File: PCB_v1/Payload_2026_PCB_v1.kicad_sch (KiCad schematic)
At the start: 9 parts, among them J1 SD Card Reader, J2 Ozone Sensor, J3 SGP40 VOC Sensor, J4 IMU, J5 BME/BMP280, J6 Ultrasonic Sensor 1, J7 Ultrasonic Sensor 2, J8 Ultrasonic Sensor 3

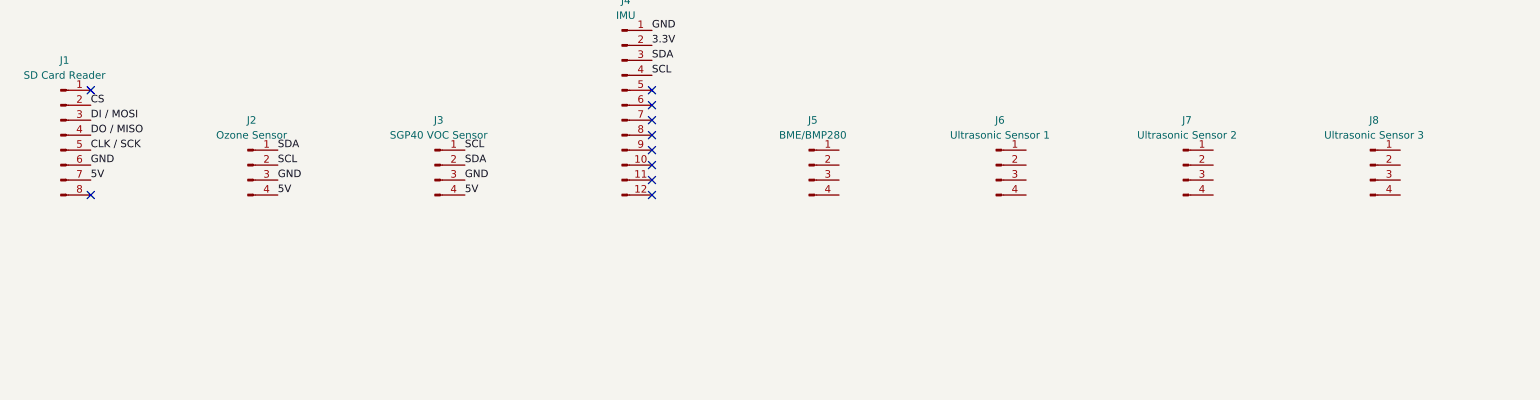
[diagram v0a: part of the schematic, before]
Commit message: PCB Footprints finished
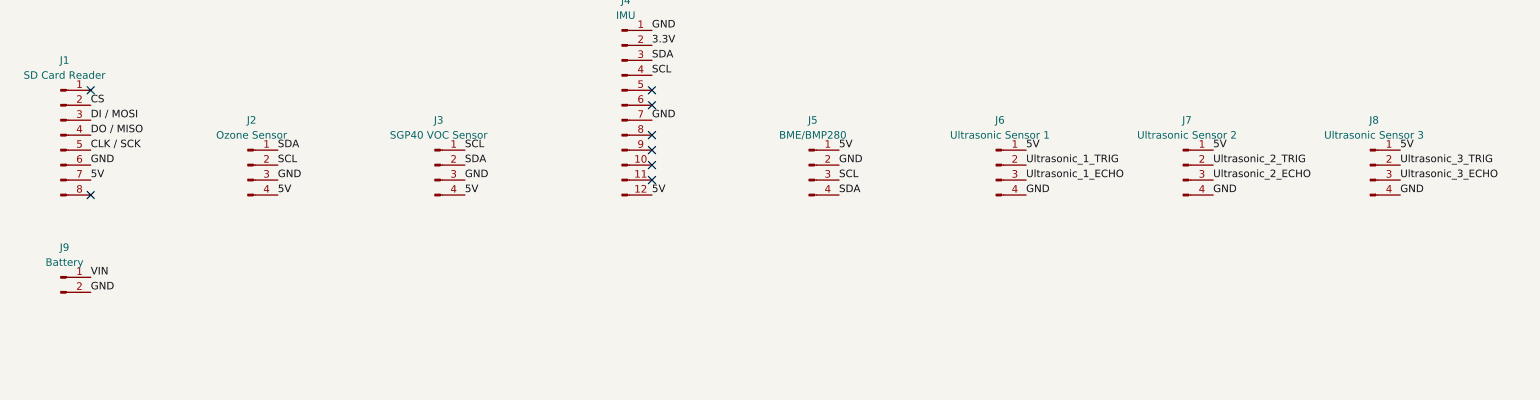
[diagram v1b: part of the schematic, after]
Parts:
- added J9: Battery, Payload_2026_PCB_v1:Battery, symbol Connector:Conn_01x02_Pin
- J1: footprint (none) -> Payload_2026_PCB_v1:SD_Card_Reader
- J2, J3, J6, J7, J8: footprint (none) -> Payload_2026_PCB_v1:Conn_01x04_Pin
- J4: footprint (none) -> Payload_2026_PCB_v1:IMU
- J5: footprint (none) -> Payload_2026_PCB_v1:BME280_Sensor
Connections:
- net 5V: now also J4.12 (Pin_12), J5.1 (Pin_1), J6.1 (Pin_1), J7.1 (Pin_1), J8.1 (Pin_1)
- net GND: now also J4.7 (Pin_7), J5.2 (Pin_2), J6.4 (Pin_4), J7.4 (Pin_4), J8.4 (Pin_4), J9.2 (Pin_2)
- net SCL: now also J5.3 (Pin_3)
- net SDA: now also J5.4 (Pin_4)
- net Ultrasonic_1_ECHO: now also J6.3 (Pin_3)
- net Ultrasonic_1_TRIG: now also J6.2 (Pin_2)
- net Ultrasonic_2_ECHO: now also J7.3 (Pin_3)
- net Ultrasonic_2_TRIG: now also J7.2 (Pin_2)
- net Ultrasonic_3_ECHO: now also J8.3 (Pin_3)
- net Ultrasonic_3_TRIG: now also J8.2 (Pin_2)
- net VIN: now also J9.1 (Pin_1)
- no-connect marks 23 -> 21

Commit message: Finish PCB Design
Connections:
- net 5V: now also J1.8 (Pin_8); no longer J1.7 (Pin_7)
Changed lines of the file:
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@@
-	)
-	(no_connect
-		(at 31.75 127)
 	)
 	(no_connect
 		(at 49.53 39.37)
+	)
+	(no_connect
+		(at 31.75 124.46)
 	)
 	(no_connect
@@
 		)
 	)
-	(label "5V"
-		(at 31.75 124.46 0)
-		(effects
-			(font
-				(size 1.27 1.27)
-			)
-			(justify left bottom)
-		)
-	)
 	(label "CS"
 		(at 31.75 111.76 0)
@@
 		)
 	)
+	(label "5V"
+		(at 31.75 127 0)
+		(effects
+			(font
+				(size 1.27 1.27)
+			)
+			(justify left bottom)
+		)
+	)

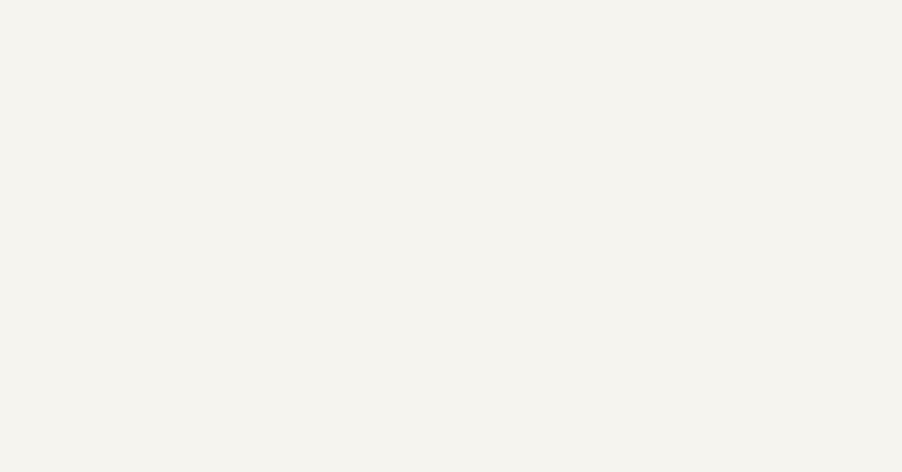
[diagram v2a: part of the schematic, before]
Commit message: Write DOTO List in sch
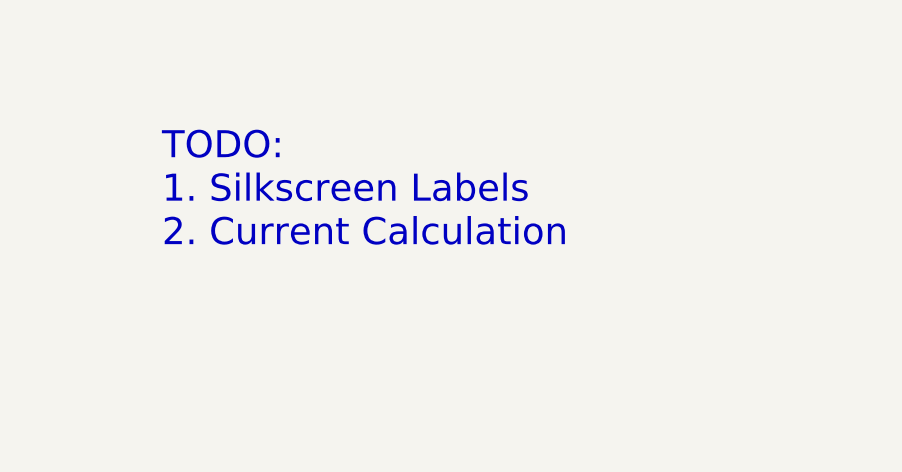
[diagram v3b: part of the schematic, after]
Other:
- note added: "TODO: 1. Silkscreen Labels 2. Current Calculation"
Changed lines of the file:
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@@
+		)
+	)
+	(text "TODO:\n1. Silkscreen Labels\n2. Current Calculation"
+		(exclude_from_sim no)
+		(at 104.648 38.862 0)
+		(effects
+			(font
+				(size 3 3)
+			)
+			(justify left top)
 		)
 	)

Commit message: Update PCB layout
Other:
- note added: "TODO: 1. Silkscreen Labels 2. Current Calculation 3. 2 Types of Pad Colors"
- note removed: "TODO: 1. Silkscreen Labels 2. Current Calculation"
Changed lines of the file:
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@@
 		)
 	)
-	(text "TODO:\n1. Silkscreen Labels\n2. Current Calculation"
+	(text "TODO:\n1. Silkscreen Labels\n2. Current Calculation\n3. 2 Types of Pad Colors"
 		(exclude_from_sim no)
 		(at 104.648 38.862 0)

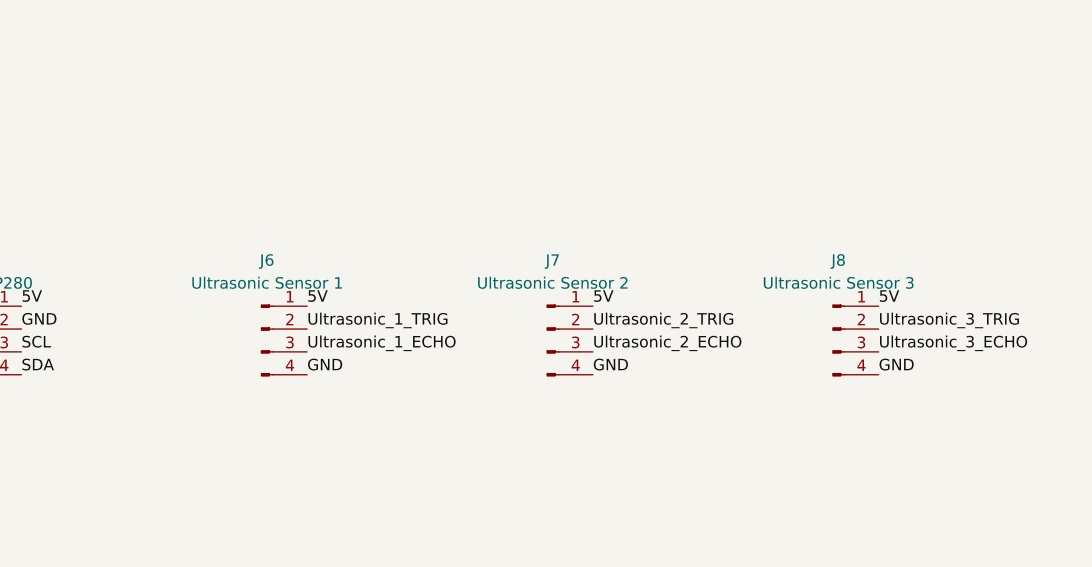
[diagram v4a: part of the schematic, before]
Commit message: Update PCB Silkscreen Labels
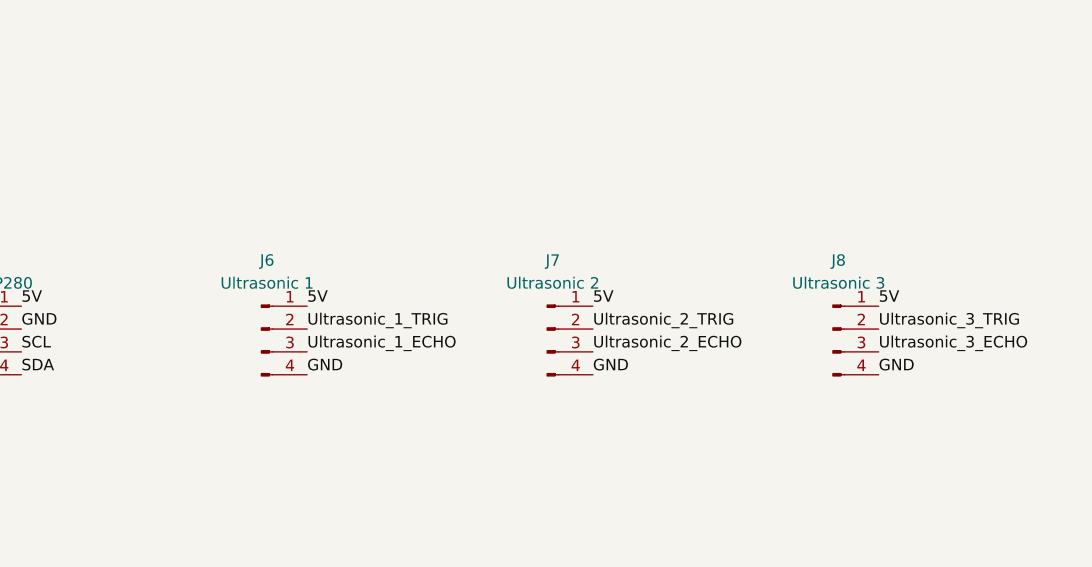
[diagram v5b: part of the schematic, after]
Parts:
- J6: value Ultrasonic Sensor 1 -> Ultrasonic 1
- J7: value Ultrasonic Sensor 2 -> Ultrasonic 2
- J8: value Ultrasonic Sensor 3 -> Ultrasonic 3
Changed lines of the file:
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@@
 			)
 		)
-		(property "Value" "Ultrasonic Sensor 2"
+		(property "Value" "Ultrasonic 2"
 			(at 217.805 116.84 0)
 			(effects
@@
 			)
 		)
-		(property "Value" "Ultrasonic Sensor 1"
+		(property "Value" "Ultrasonic 1"
 			(at 186.055 116.84 0)
 			(effects
@@
 			)
 		)
-		(property "Value" "Ultrasonic Sensor 3"
+		(property "Value" "Ultrasonic 3"
 			(at 249.555 116.84 0)
 			(effects

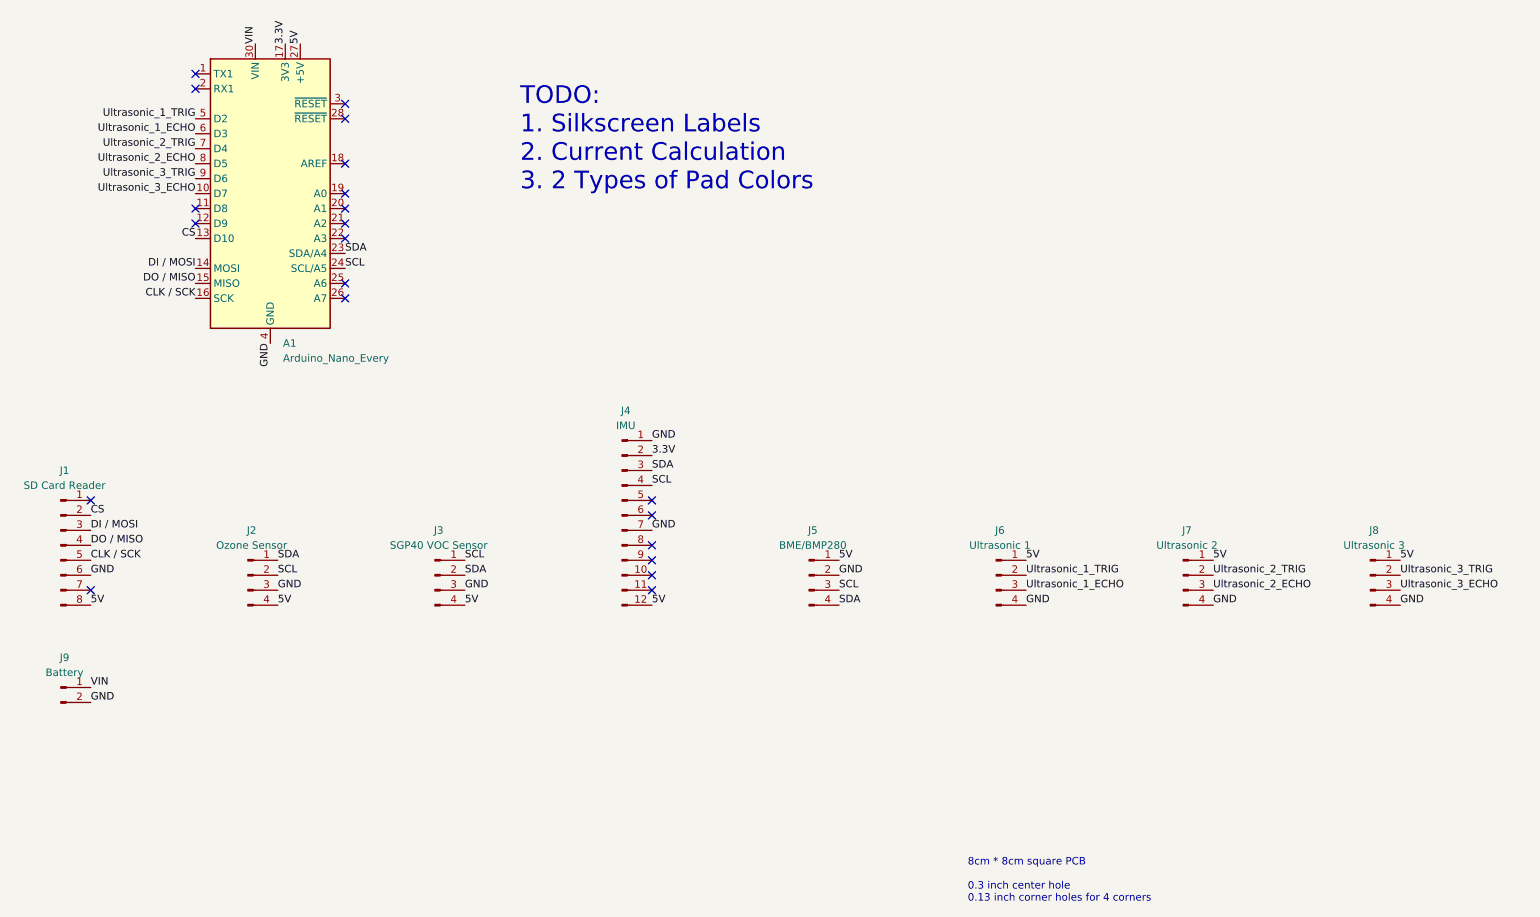
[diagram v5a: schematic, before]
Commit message: Add SW-18020P to the PCB; generate gerber files
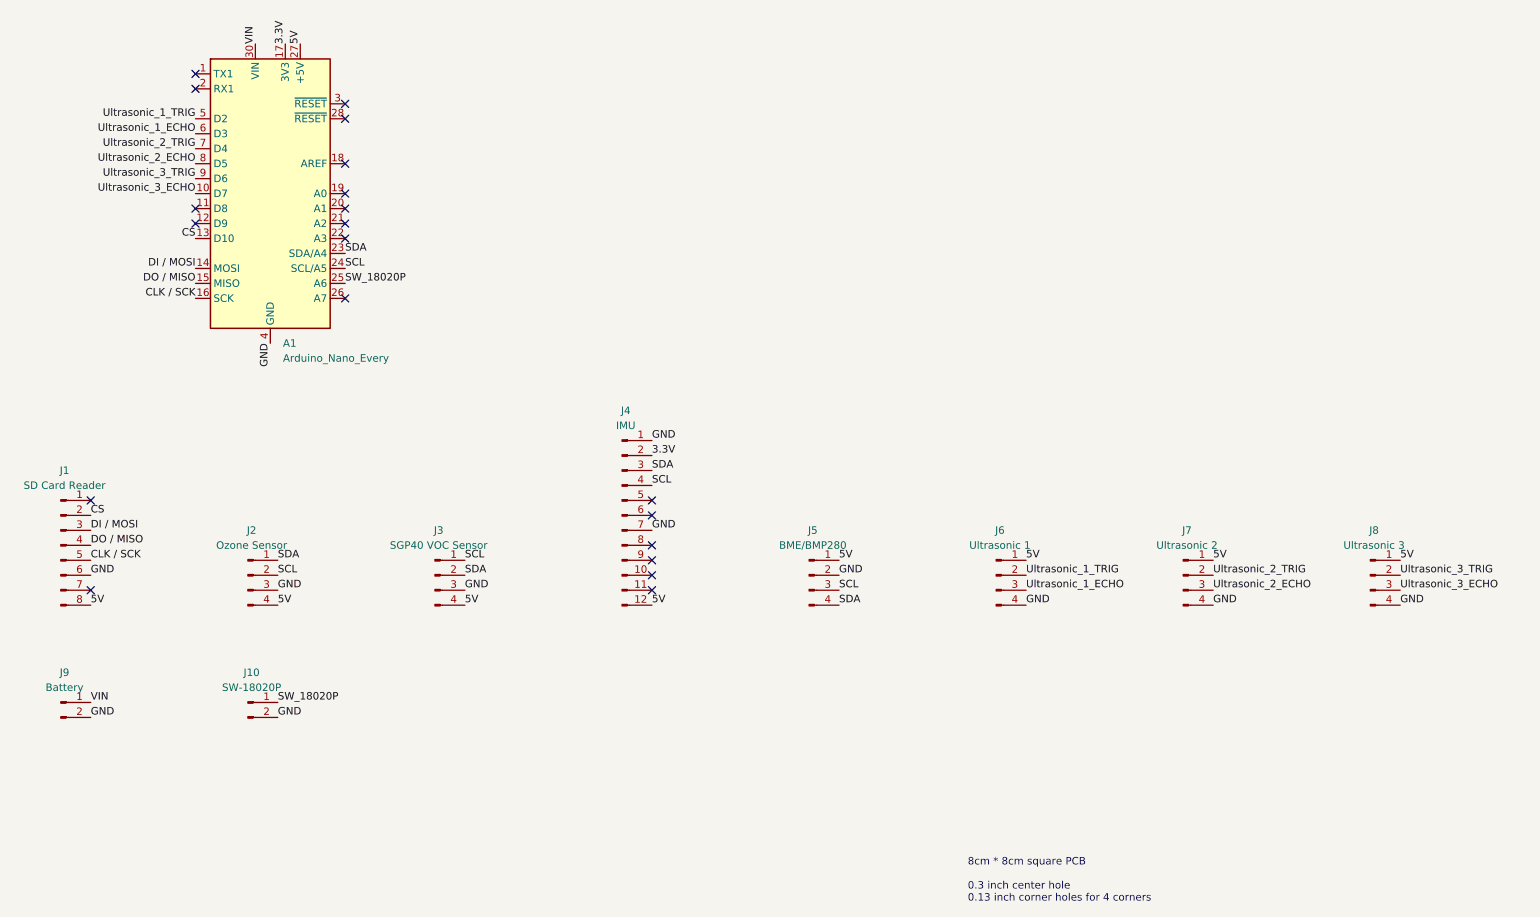
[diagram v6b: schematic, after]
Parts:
- added J10: SW-18020P, Payload_2026_PCB_v1:SW_18020P, symbol Connector:Conn_01x02_Pin
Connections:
- net GND: now also J10.2 (Pin_2)
- net SW_18020P: now reaches A1.25 (A6)
- net SW_18020P: now also J10.1 (Pin_1)
- no-connect marks 21 -> 20
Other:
- note removed: "TODO: 1. Silkscreen Labels 2. Current Calculation 3. 2 Types of Pad Colors"
- moved on the sheet: J9
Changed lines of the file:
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@@
-		)
-	)
-	(text "TODO:\n1. Silkscreen Labels\n2. Current Calculation\n3. 2 Types of Pad Colors"
-		(exclude_from_sim no)
-		(at 104.648 38.862 0)
-		(effects
-			(font
-				(size 3 3)
-			)
-			(justify left top)
 		)
 	)
@@
 	(no_connect
 		(at 74.93 59.69)
-	)
-	(no_connect
-		(at 74.93 72.39)
 	)
 	(no_connect
@@
 		)
 	)
+	(label "SW_18020P"
+		(at 74.93 72.39 0)
+		(effects
+			(font
+				(size 1.27 1.27)
+			)
+			(justify left bottom)
+		)
+	)
 	(label "SDA"
 		(at 127 104.14 0)
@@
 	)
 	(label "VIN"
-		(at 31.75 140.97 0)
+		(at 31.75 143.51 0)
 		(effects
 			(font
@@
 	)
 	(label "GND"
-		(at 31.75 143.51 0)
+		(at 31.75 146.05 0)
 		(effects
 			(font
@@
 	(label "GND"
 		(at 95.25 124.46 0)
+		(effects
+			(font
+				(size 1.27 1.27)
+			)
+			(justify left bottom)
+		)
+	)
+	(label "GND"
+		(at 63.5 146.05 0)
+		(effects
+			(font
+				(size 1.27 1.27)
+			)
+			(justify left bottom)
+		)
+	)
+	(label "SW_18020P"
+		(at 63.5 143.51 0)
 		(effects
 			(font
@@
 	)
 	(symbol
+		(lib_id "Connector:Conn_01x02_Pin")
+		(at 58.42 143.51 0)
+		(unit 1)
+		(exclude_from_sim no)
+		(in_bom yes)
+		(on_board yes)
+		(dnp no)
+		(fields_autoplaced yes)
+		(property "Reference" "J10"
+			(at 59.055 138.43 0)
+			(effects
+				(font
+					(size 1.27 1.27)
+				)
+			)
+		)
+		(property "Value" "SW-18020P"
+			(at 59.055 140.97 0)
+			(effects
+				(font
+					(size 1.27 1.27)
+				)
+			)
+		)
+		(property "Footprint" "Payload_2026_PCB_v1:SW_18020P"
+			(at 58.42 143.51 0)
+			(effects
+				(font
+					(size 1.27 1.27)
+				)
+				(hide yes)
+			)
+		)
+		(property "Datasheet" "~"
+			(at 58.42 143.51 0)
+			(effects
+				(font
+					(size 1.27 1.27)
+				)
+				(hide yes)
+			)
+		)
+		(property "Description" "Generic connector, single row, 01x02, script generated"
+			(at 58.42 143.51 0)
+			(effects
+				(font
+					(size 1.27 1.27)
+				)
+				(hide yes)
+			)
+		)
+		(pin "2"
+		)
+		(pin "1"
+		)
+		(instances
+			(project "Payload_2026_PCB_v1"
+				(path "/7e572a3c-507c-47f6-a212-f5f78d2e5847"
+					(reference "J10")
+					(unit 1)
+				)
+			)
+		)
+	)
+	(symbol
 		(lib_id "Connector:Conn_01x08_Pin")
 		(at 26.67 116.84 0)
@@
 	(symbol
 		(lib_id "Connector:Conn_01x02_Pin")
-		(at 26.67 140.97 0)
+		(at 26.67 143.51 0)
 		(unit 1)
 		(exclude_from_sim no)
@@
 		(fields_autoplaced yes)
 		(property "Reference" "J9"
-			(at 27.305 135.89 0)
+			(at 27.305 138.43 0)
 			(effects
 				(font
@@
 		)
 		(property "Value" "Battery"
-			(at 27.305 138.43 0)
+			(at 27.305 140.97 0)
 			(effects
 				(font
@@
 		)
 		(property "Footprint" "Payload_2026_PCB_v1:Battery"
-			(at 26.67 140.97 0)
+			(at 26.67 143.51 0)
 			(effects
 				(font
@@
 		)
 		(property "Datasheet" "~"
-			(at 26.67 140.97 0)
+			(at 26.67 143.51 0)
 			(effects
 				(font
@@
 		)
 		(property "Description" "Generic connector, single row, 01x02, script generated"
-			(at 26.67 140.97 0)
-			(effects
-				(font
+			(at 26.67 143.51 0)
+			(effects
+				(font
